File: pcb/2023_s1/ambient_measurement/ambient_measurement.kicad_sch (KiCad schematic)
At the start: 12 parts, among them J1 Screw_Terminal_01x03, J2 Screw_Terminal_01x04, U1 NRF24L01_Breakout

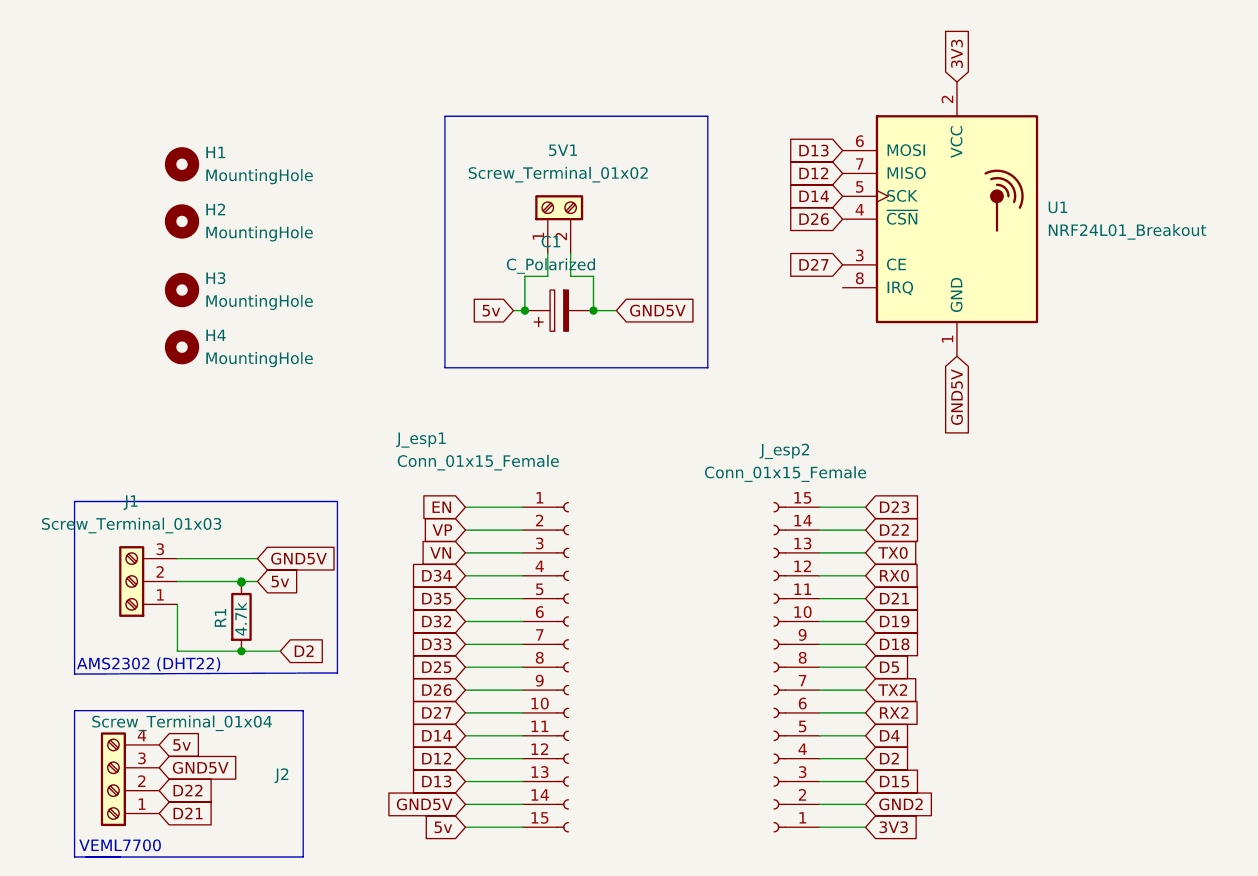
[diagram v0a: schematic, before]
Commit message: update, changed the dht22 pin from 2 to 25, added a ceramic capacitor, and rerouted some elements
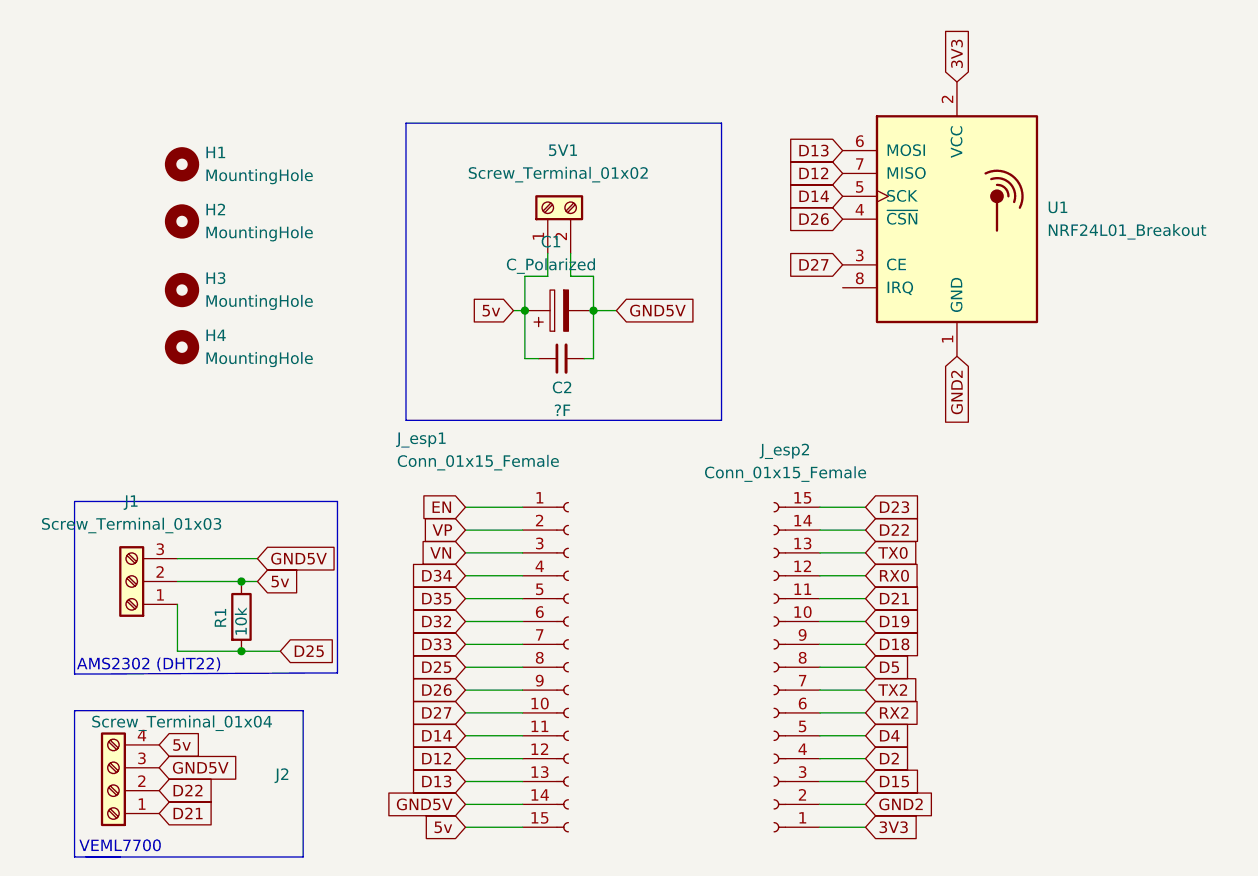
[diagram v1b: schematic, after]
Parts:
- added C2: C_Generic, Capacitor_THT:C_Disc_D5.0mm_W2.5mm_P2.50mm, symbol PCM_4ms_Capacitor:C_Generic
- R1: value 4.7k -> 10k
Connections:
- net 5v: now also C2.1
- net D2: no longer J1.1 (Pin_1), R1.2
- net D25: now also J1.1 (Pin_1), R1.2
- net GND2: now also U1.1 (GND)
- net GND5V: now also C2.2; no longer U1.1 (GND)

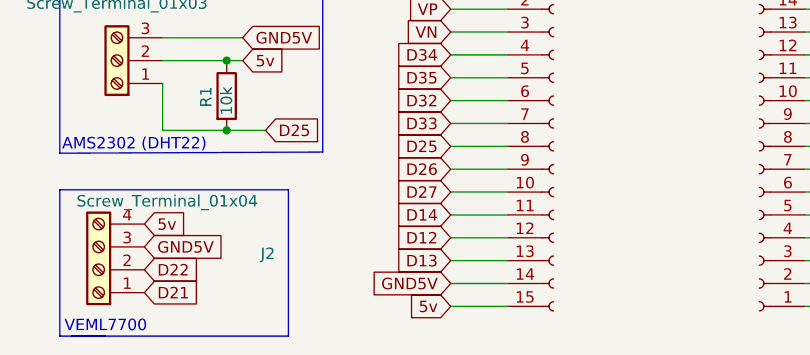
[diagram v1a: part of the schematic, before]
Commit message: update, repositioned sensors and rf module so we can use shorter tracks and looks better
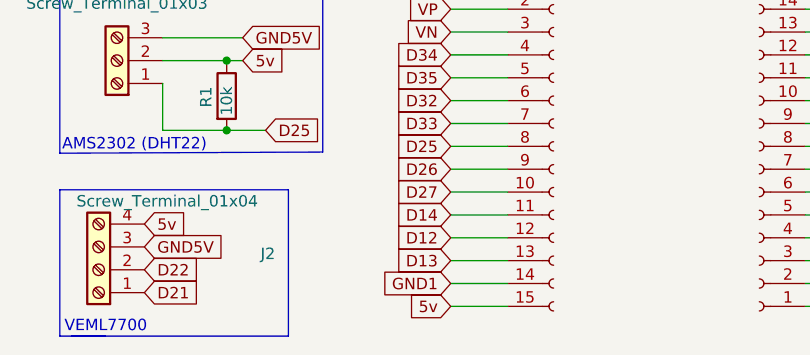
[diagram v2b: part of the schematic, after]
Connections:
- net GND5V: no longer J_esp1.14 (Pin_14)
- new net GND1: J_esp1.14 (Pin_14)
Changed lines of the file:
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@@
     )
   )
-  (global_label "GND5V" (shape input) (at 145.542 115.57 180) (fields_autoplaced)
+  (global_label "GND1" (shape input) (at 145.542 115.57 180) (fields_autoplaced)
     (effects (font (size 1.27 1.27)) (justify right))
-    (property "Intersheetrefs" "${INTERSHEET_REFS}" (at 136.9603 115.6494 0)
+    (property "Intersheetrefs" "${INTERSHEET_REFS}" (at 137.5562 115.57 0)
       (effects (font (size 1.27 1.27)) (justify right) hide)
     )
